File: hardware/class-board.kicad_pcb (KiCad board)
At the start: 4 copper layers, 180 x 100 mm, 334 parts, among them J1 DevKit J1 (left row), J10 C2937625_-_Conn_01x03, J11 C2937625_-_Conn_01x03, J12 C2937625_-_Conn_01x03, J13 C492401-PZ254V-11-02P, J14 C2937625_-_Conn_01x03, J15 C2937625_-_Conn_01x03, J2 DevKit J3 (right row), J201 USB-C 16P, J202 DC005-T20, J3 C2937625_-_Conn_01x03, J4 Qwiic, J5 Expansion 2x10, J6 Panel link 2x20 female, J7 Panel link 2x20 female, J8 Panel link 2x20 female, J9 C2937625_-_Conn_01x03, J901 KF301-5.0-2P, J903 KF301-5.0-2P, J905 KF301-5.0-3P, Q901 AOD4185, Q904 AOD4184A, U101 ADS8688IDBTR, U201 LM66100DCKR, U202 LM66100DCKR, U203 78L05G-AB3-R, U204 AMS1117-3.3, U301 DAC8563SDGSR, U302 74HCT125PW, U303 OPA2192IDR, U501 SN74AHCT541PWR, U502 74HCT125PW, U503 SN74LVC1T45DBVR, U505 TCA9535PWR, U701 SI5351A-B-GT, U702 74HC74D,653, U703 OPA1656IDR, U704 DG419DY-T1-E3, U705 OPA1612AIDR, U706 OPA1612AIDR, U801 AD9834BRUZ, U802 OPA564AIDWPR, U901 TS5A23157DGSR, U902 TS5A23157DGSR, U903 DRV8871DDAR, U904 UCC27517DBVR, Y701 25 MHz

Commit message: Main board divided into four routing AREAS (instructor, 2026-09-21): rule areas ZONE_A..D in the master, main_sections.py areas/split/check/merge/report, sections/{A,B,C,D} student copies with the instructor's routing locked, owner_* Block-field rules retired; docs
Co-Authored-By: Claude Fable 5.1 <noreply@anthropic.com>
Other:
- board text added: "AREA A"
- board text added: "AREA B"
- board text added: "AREA C"
- board text added: "AREA D"
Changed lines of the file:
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@@
-	)
-	(zone
-		(layer "F.Cu")
-		(name "ZONE_A")
-		(hatch edge 0.5)
-		(connect_pads
-			(clearance 0)
-		)
-		(min_thickness 0.25)
-		(keepout
-			(tracks allowed)
-			(vias allowed)
-			(pads allowed)
-			(copperpour allowed)
-			(footprints allowed)
-		)
-		(placement
-			(enabled no)
-			(sheetname "")
-		)
-		(fill
-			(thermal_gap 0.5)
-			(thermal_bridge_width 0.5)
-			(island_removal_mode 0)
-		)
-		(polygon
-			(pts
-				(xy 0.5 72.5) (xy 45 72.5) (xy 45 72) (xy 100 72) (xy 100 86) (xy 113 86) (xy 113 114.5) (xy 0.5 114.5)
-			)
-		)
 	)
 	(zone
@@
 	)
 	(zone
-		(layer "F.Cu")
-		(name "ZONE_B")
-		(hatch edge 0.5)
-		(connect_pads
-			(clearance 0)
-		)
-		(min_thickness 0.25)
-		(keepout
-			(tracks allowed)
-			(vias allowed)
-			(pads allowed)
-			(copperpour allowed)
-			(footprints allowed)
-		)
-		(placement
-			(enabled no)
-			(sheetname "")
-		)
-		(fill
-			(thermal_gap 0.5)
-			(thermal_bridge_width 0.5)
-			(island_removal_mode 0)
-		)
-		(polygon
-			(pts
-				(xy 96 15.5) (xy 179.5 15.5) (xy 179.5 114.5) (xy 113 114.5) (xy 113 86) (xy 100 86) (xy 100 51)
-				(xy 96 51)
-			)
-		)
-	)
-	(zone
-		(layer "F.Cu")
-		(name "ZONE_INSTR")
-		(hatch edge 0.5)
-		(connect_pads
-			(clearance 0)
-		)
-		(min_thickness 0.25)
-		(keepout
-			(tracks allowed)
-			(vias allowed)
-			(pads allowed)
-			(copperpour allowed)
-			(footprints allowed)
-		)
-		(placement
-			(enabled no)
-			(sheetname "")
-		)
-		(fill
-			(thermal_gap 0.5)
-			(thermal_bridge_width 0.5)
-			(island_removal_mode 0)
-		)
-		(polygon
-			(pts
-				(xy 0.5 15.5) (xy 96 15.5) (xy 96 51) (xy 37.5 51) (xy 37.5 72.5) (xy 0.5 72.5)
-			)
-		)
-	)
-	(zone
 		(net "/c_switch/HB_OUT1")
 		(layer "F.Cu")
@@
 				(xy 88.45 33) (xy 93.45 33) (xy 93.45 29.4) (xy 89.861703 29.377344) (xy 89.8865 25.45) (xy 89.8865 16.7)
 				(xy 82.7 16.9) (xy 82.7 22.55) (xy 88 25.05) (xy 88.1 29.25)
-			)
-		)
-	)
-	(zone
-		(layer "F.Cu")
-		(name "ZONE_BASE")
-		(hatch edge 0.5)
-		(connect_pads
-			(clearance 0)
-		)
-		(min_thickness 0.25)
-		(keepout
-			(tracks allowed)
-			(vias allowed)
-			(pads allowed)
-			(copperpour allowed)
-			(footprints allowed)
-		)
-		(placement
-			(enabled no)
-			(sheetname "")
-		)
-		(fill
-			(thermal_gap 0.5)
-			(thermal_bridge_width 0.5)
-			(island_removal_mode 0)
-		)
-		(polygon
-			(pts
-				(xy 37.5 51) (xy 100 51) (xy 100 72) (xy 37.5 72)
 			)
 		)
@@
 	)
 	(embedded_fonts no)
+	(zone
+		(net 0)
+		(net_name "")
+		(layers "F.Cu" "B.Cu")
+		(name "ZONE_A")
+		(hatch edge 0.5)
+		(connect_pads
+			(clearance 0)
+		)
+		(min_thickness 0.25)
+		(keepout
+			(tracks allowed)
+			(vias allowed)
+			(pads allowed)
+			(copperpour allowed)
+			(footprints allowed)
+		)
+		(placement
+			(enabled no)
+			(sheetname "")
+		)
+		(fill
+			(thermal_gap 0.5)
+			(thermal_bridge_width 0.5)
+			(island_removal_mode 0)
+		)
+		(polygon
+			(pts
+				(xy 96 15.5) (xy 179.5 15.5) (xy 179.5 59.5) (xy 109 59.5) (xy 109 52) (xy 96 52)
+			)
+		)
+	)
+	(gr_text "AREA A"
+		(at 97 16.2 0)
+		(layer "Cmts.User")
+		(effects
+			(font
+				(size 2 2)
+				(thickness 0.25)
+			)
+			(justify left)
+		)
+	)
+	(zone
+		(net 0)
+		(net_name "")
+		(layers "F.Cu" "B.Cu")
+		(name "ZONE_B")
+		(hatch edge 0.5)
+		(connect_pads
+			(clearance 0)
+		)
+		(min_thickness 0.25)
+		(keepout
+			(tracks allowed)
+			(vias allowed)
+			(pads allowed)
+			(copperpour allowed)
+			(footprints allowed)
+		)
+		(placement
+			(enabled no)
+			(sheetname "")
+		)
+		(fill
+			(thermal_gap 0.5)
+			(thermal_bridge_width 0.5)
+			(island_removal_mode 0)
+		)
+		(polygon
+			(pts
+				(xy 109 59.5) (xy 179.5 59.5) (xy 179.5 114.5) (xy 109 114.5)
+			)
+		)
+	)
+	(gr_text "AREA B"
+		(at 110.5 60.5 0)
+		(layer "Cmts.User")
+		(effects
+			(font
+				(size 2 2)
+				(thickness 0.25)
+			)
+			(justify left)
+		)
+	)
+	(zone
+		(net 0)
+		(net_name "")
+		(layers "F.Cu" "B.Cu")
+		(name "ZONE_C")
+		(hatch edge 0.5)
+		(connect_pads
+			(clearance 0)
+		)
+		(min_thickness 0.25)
+		(keepout
+			(tracks allowed)
+			(vias allowed)
+			(pads allowed)
+			(copperpour allowed)
+			(footprints allowed)
+		)
+		(placement
+			(enabled no)
+			(sheetname "")
+		)
+		(fill
+			(thermal_gap 0.5)
+			(thermal_bridge_width 0.5)
+			(island_removal_mode 0)
+		)
+		(polygon
+			(pts
+				(xy 0.5 75) (xy 109 75) (xy 109 114.5) (xy 0.5 114.5)
+			)
+		)
+	)
+	(gr_text "AREA C"
+		(at 45 76 0)
+		(layer "Cmts.User")
+		(effects
+			(font
+				(size 2 2)
+				(thickness 0.25)
+			)
+			(justify left)
+		)
+	)
+	(zone
+		(net 0)
+		(net_name "")
+		(layers "F.Cu" "B.Cu")
+		(name "ZONE_D")
+		(hatch edge 0.5)
+		(connect_pads
+			(clearance 0)
+		)
+		(min_thickness 0.25)
+		(keepout
+			(tracks allowed)
+			(vias allowed)
+			(pads allowed)
+			(copperpour allowed)
+			(footprints allowed)
+		)
+		(placement
+			(enabled no)
+			(sheetname "")
+		)
+		(fill
+			(thermal_gap 0.5)
+			(thermal_bridge_width 0.5)
+			(island_removal_mode 0)
+		)
+		(polygon
+			(pts
+				(xy 0.5 15.5) (xy 96 15.5) (xy 96 52) (xy 109 52) (xy 109 75) (xy 0.5 75)
+			)
+		)
+	)
+	(gr_text "AREA D"
+		(at 3 49.5 0)
+		(layer "Cmts.User")
+		(effects
+			(font
+				(size 2 2)
+				(thickness 0.25)
+			)
+			(justify left)
+		)
+	)
 )

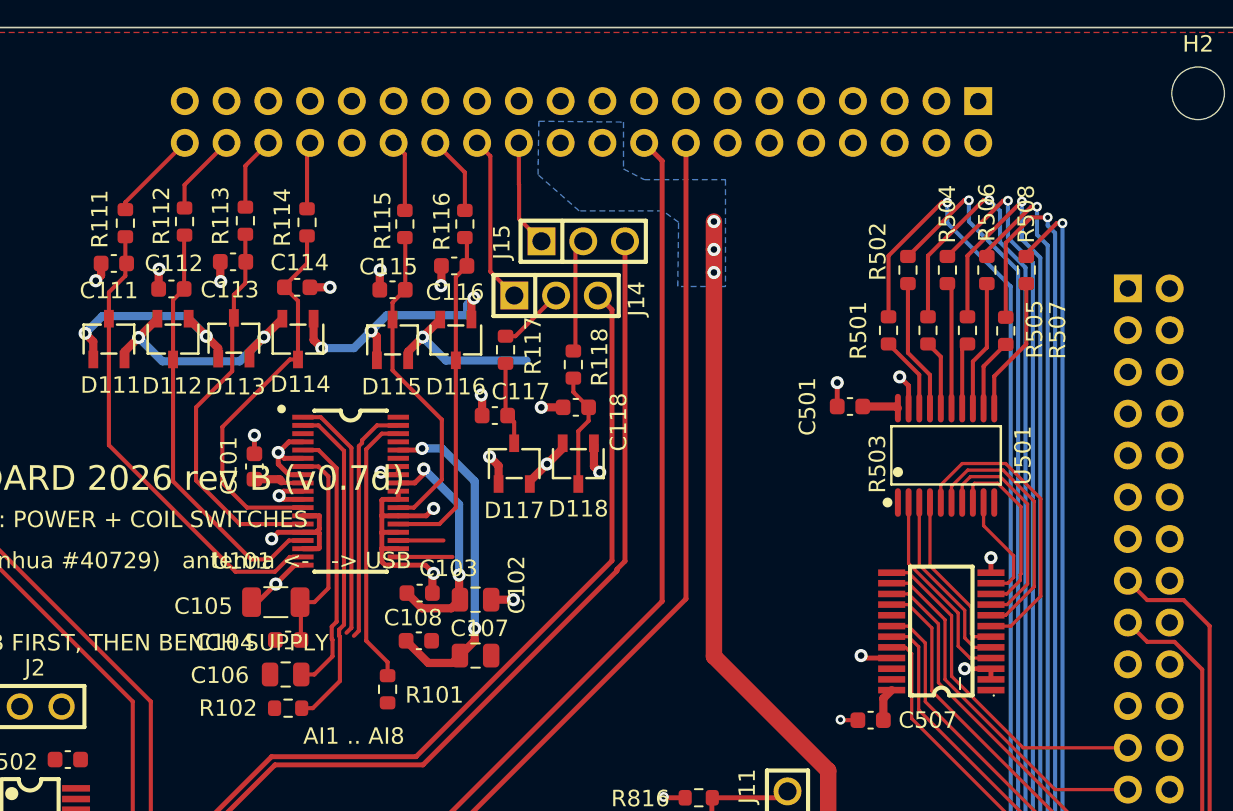
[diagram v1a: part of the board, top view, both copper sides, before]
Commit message: Merge student A (Renqian): area A of the main board (417 tracks/vias, unconnected 197 -> 148) and panel section A (13 analog nets, 121 unconnected left) accepted into the masters; sections re-split
Co-Authored-By: Claude Fable 5.1 <noreply@anthropic.com>
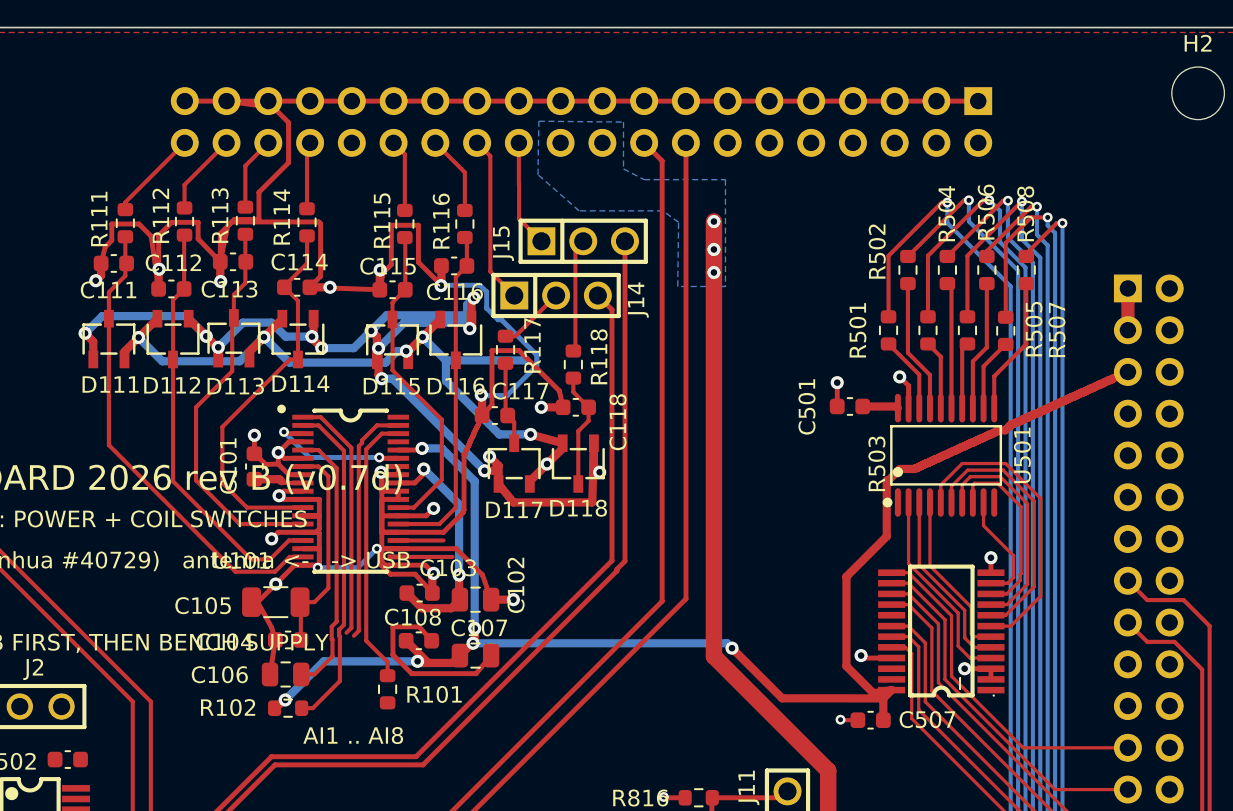
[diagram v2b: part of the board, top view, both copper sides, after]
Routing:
- net AGND: track 162.8 -> 342.1 mm, vias 87 -> 89
- net +3V3: track 77.5 -> 147.6 mm, vias 6 -> 10
- net -12V: track 80.5 -> 115.1 mm, vias 11 -> 17
- net GND: track 135.3 -> 155.5 mm, vias 68 -> 70
- net +12V: track 94.6 -> 114.1 mm, vias 9 -> 11
- net +5V_RAW: track 86.6 -> 89.1 mm

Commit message: WIP masters (instructor), 2026-09-24 14:26
Co-Authored-By: Claude Fable 5.1 <noreply@anthropic.com>
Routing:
- net AGND: track 342.1 -> 312.6 mm, vias 89 -> 87
- net /b1_inputs/CS_ADC: track 0.00 -> 10.8 mm
- net +5VA: track 34.4 -> 44.9 mm, vias 2 -> 3
- net GND: track 155.5 -> 154.3 mm, vias 70 -> 69
- removed copper zone on B.Cu, net AGND
- removed copper zone on F.Cu, net AGND
- removed copper zone on F.Cu, net GND
- removed copper zone on In1.Cu, net GND
- removed copper zone on In2.Cu, net GND
